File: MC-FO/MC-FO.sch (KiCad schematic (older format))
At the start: 1 part, among them J1 DB25_Female

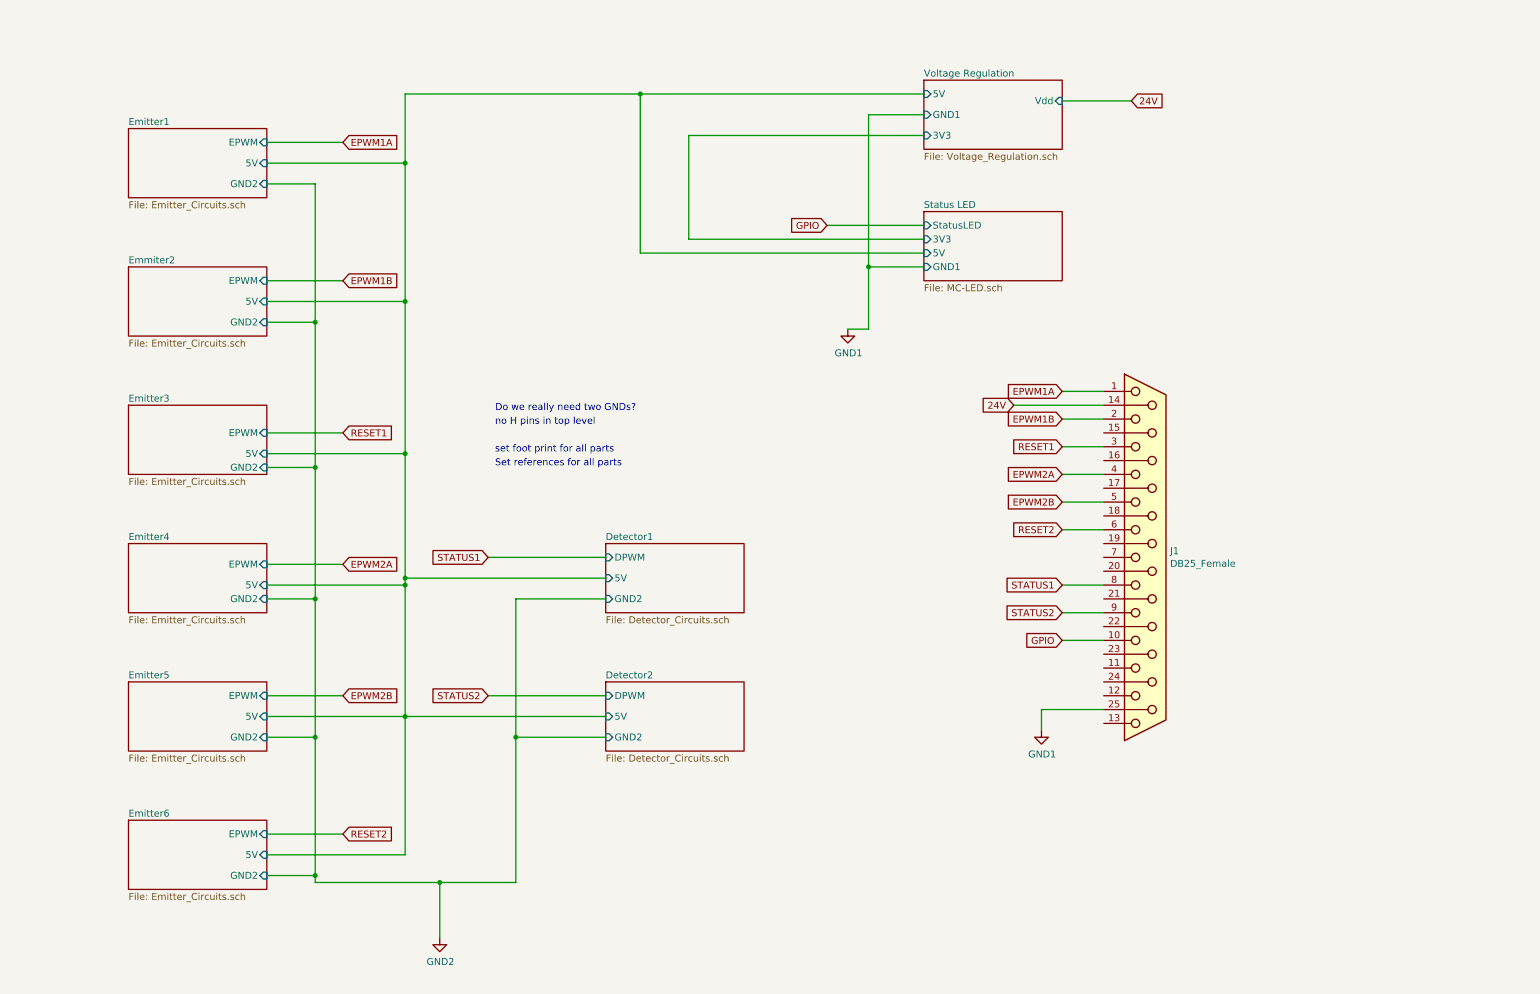
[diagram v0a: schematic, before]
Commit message: unpopulated cap after voltage regulators
and changed reference designator numbering scheme
and moved the or gate that sends 3.3 V to comparator in detector ckt
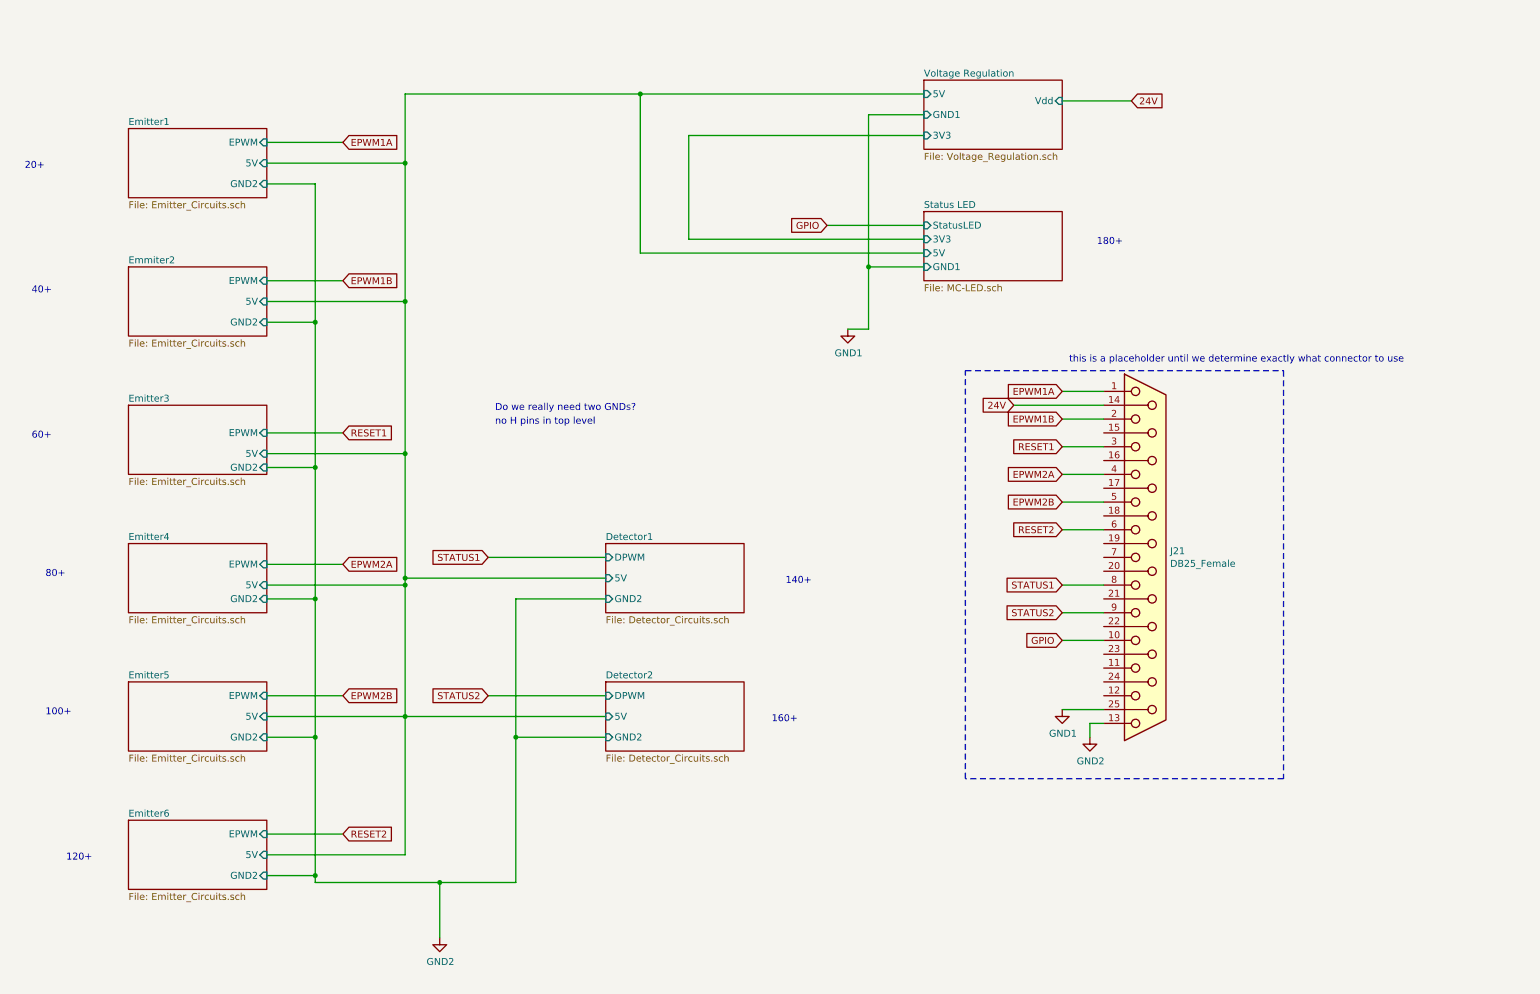
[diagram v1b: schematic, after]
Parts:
- renumbered J1 to J21
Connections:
- net GND2: now also J21.13
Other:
- note added: "100+"
- note added: "120+"
- note added: "140+"
- note added: "160+"
- note added: "180+"
- note added: "20+"
- note added: "40+"
- note added: "60+"
- note added: "80+"
- note added: "this is a placeholder until we determine exactly what connector to use"
- note removed: "Set references for all parts\n"
- note removed: "set foot print for all parts\n"
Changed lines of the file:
@@
 24V
 $Comp
-L Connector:DB25_Female J1
+L Connector:DB25_Female J21
 U 1 1 6179E2FC
 P 8850 4600
-F 0 "J1" H 9030 4646 50  0000 L CNN
+F 0 "J21" H 9030 4646 50  0000 L CNN
 F 1 "DB25_Female" H 9030 4555 50  0000 L CNN
 F 2 "Connector_Dsub:DSUB-25_Female_Horizontal_P2.77x2.54mm_EdgePinOffset9.40mm" H 8850 4600 50  0001 C CNN
@@
 	1    0    0    -1
 $EndComp
-Text Notes 4150 3850 0    50   ~ 0
-set foot print for all parts\n
-Text Notes 4150 3950 0    50   ~ 0
-Set references for all parts\n
 Text GLabel 8250 3800 0    50   Input ~ 0
 RESET1
@@
 Wire Wire Line
 	8550 5200 8250 5200
-Wire Wire Line
-	8100 5700 8550 5700
-Wire Wire Line
-	8100 5700 8100 5850
 Text GLabel 4100 4600 0    50   Input ~ 0
 STATUS1
@@
 Connection ~ 3500 2750
 $Comp
-L power:GND1 #PWR02
+L power:GND1 #PWR022
 U 1 1 617AD6F4
 P 6700 2950
-F 0 "#PWR02" H 6700 2700 50  0001 C CNN
+F 0 "#PWR022" H 6700 2700 50  0001 C CNN
 F 1 "GND1" H 6705 2777 50  0000 C CNN
 F 2 "" H 6700 2950 50  0001 C CNN
@@
 $EndComp
 $Comp
-L power:GND2 #PWR01
+L power:GND2 #PWR021
 U 1 1 617AF034
 P 3750 7350
-F 0 "#PWR01" H 3750 7100 50  0001 C CNN
+F 0 "#PWR021" H 3750 7100 50  0001 C CNN
 F 1 "GND2" H 3755 7177 50  0000 C CNN
 F 2 "" H 3750 7350 50  0001 C CNN
 F 3 "" H 3750 7350 50  0001 C CNN
 	1    3750 7350
-	1    0    0    -1
-$EndComp
-$Comp
-L power:GND1 #PWR03
-U 1 1 617AF950
-P 8100 5850
-F 0 "#PWR03" H 8100 5600 50  0001 C CNN
-F 1 "GND1" H 8105 5677 50  0000 C CNN
-F 2 "" H 8100 5850 50  0001 C CNN
-F 3 "" H 8100 5850 50  0001 C CNN
-	1    8100 5850
 	1    0    0    -1
 $EndComp
@@
 Wire Wire Line
 	2500 1600 3050 1600
+$Comp
+L power:GND1 #PWR023
+U 1 1 617AF950
+P 8250 5700
+F 0 "#PWR023" H 8250 5450 50  0001 C CNN
+F 1 "GND1" H 8255 5527 50  0000 C CNN
+F 2 "" H 8250 5700 50  0001 C CNN
+F 3 "" H 8250 5700 50  0001 C CNN
+	1    8250 5700
+	1    0    0    -1
+$EndComp
+Wire Wire Line
+	8250 5700 8550 5700
+Text Notes 8300 3200 0    50   ~ 0
+this is a placeholder until we determine exactly what connector to use
+Wire Notes Line
+	7550 3250 9850 3250
+Wire Notes Line
+	9850 3250 9850 6200
+Wire Notes Line
+	9850 6200 7550 6200
+Wire Notes Line
+	7550 6200 7550 3250
+Wire Wire Line
+	8550 5800 8450 5800
+Wire Wire Line
+	8450 5800 8450 5900
+$Comp
+L power:GND2 #PWR0102
+U 1 1 61820807
+P 8450 5900
+F 0 "#PWR0102" H 8450 5650 50  0001 C CNN
+F 1 "GND2" H 8455 5727 50  0000 C CNN
+F 2 "" H 8450 5900 50  0001 C CNN
+F 3 "" H 8450 5900 50  0001 C CNN
+	1    8450 5900
+	1    0    0    -1
+$EndComp
+Text Notes 750  1800 0    50   ~ 0
+20+
+Text Notes 800  2700 0    50   ~ 0
+40+
+Text Notes 800  3750 0    50   ~ 0
+60+
+Text Notes 900  4750 0    50   ~ 0
+80+
+Text Notes 900  5750 0    50   ~ 0
+100+
+Text Notes 1050 6800 0    50   ~ 0
+120+
+Text Notes 6250 4800 0    50   ~ 0
+140+
+Text Notes 6150 5800 0    50   ~ 0
+160+
+Text Notes 8500 2350 0    50   ~ 0
+180+
 $EndSCHEMATC

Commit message: Fixed file hierarchy
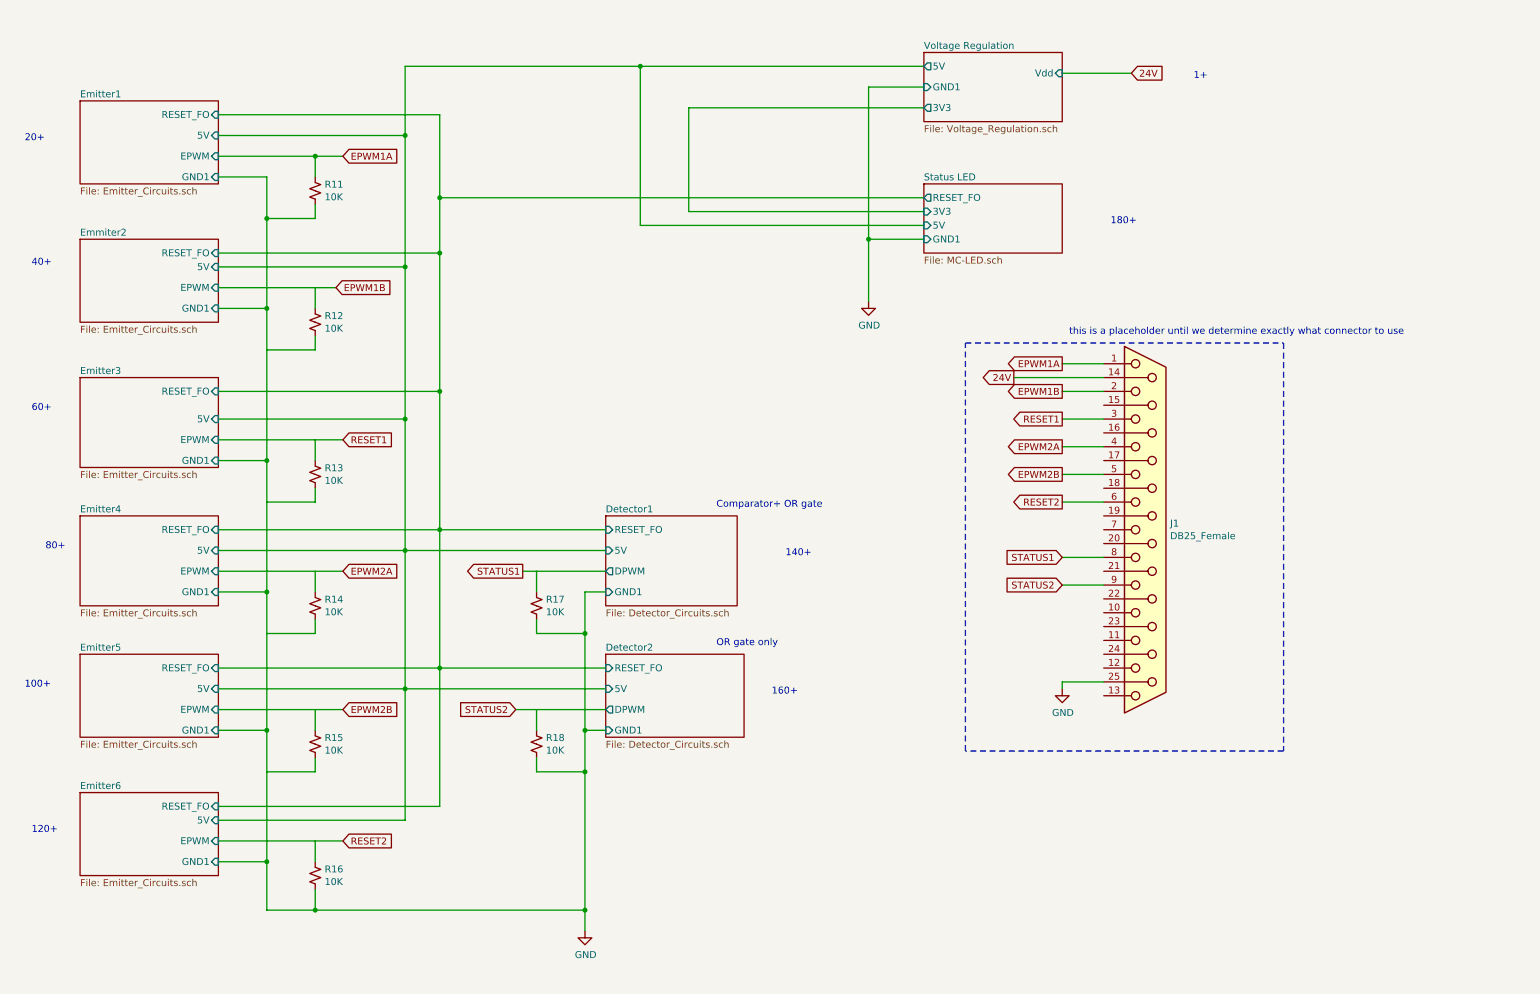
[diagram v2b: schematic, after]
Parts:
- added R11, R12, R13, R14, R15, R16, R17, R18: 10K, Resistor_SMD:R_0603_1608Metric, symbol Device:R_Small_US
- renumbered J21 to J1
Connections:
- net labels added: GND
- net labels removed: GND1, GND2, GPIO
- wire segments 69 -> 106
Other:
- note added: "1+"
- note added: "Comparator+ OR gate"
- note added: "OR gate only"
- note removed: "Do we really need two GNDs?"
- note removed: "no H pins in top level\n"
- moved on the sheet: J1

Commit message: Detector2 update, RESET integration
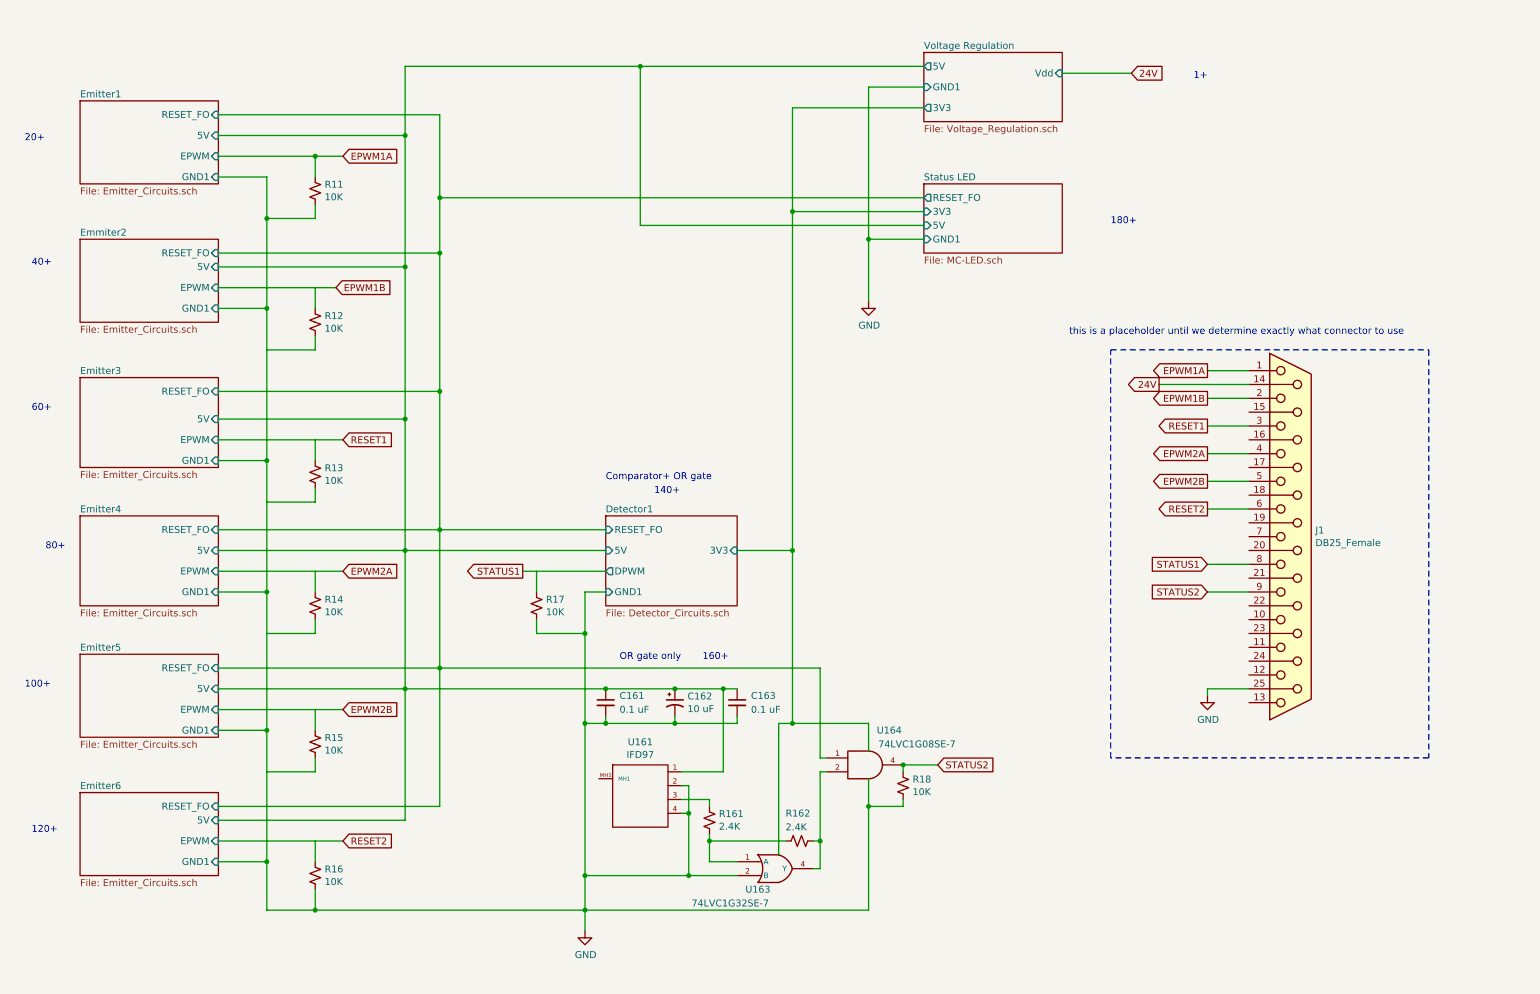
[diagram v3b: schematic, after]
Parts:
- added C161, C163: 0.1 uF, Capacitor_SMD:C_0603_1608Metric, symbol Device:C_Small
- added C162: 10 uF, Capacitor_SMD:C_0603_1608Metric, symbol Device:CP1_Small
- added R161, R162: 2.4K, Resistor_SMD:R_0603_1608Metric, symbol Device:R_Small_US
- added U161: IFD97, symbol Existing_IC_Models:IFD97
- added U163: 74LVC1G32SE-7, Package_TO_SOT_SMD:SOT-353_SC-70-5, symbol Existing_IC_Models:74LVC1G32SE-7
- added U164: 74LVC1G08SE-7, Package_TO_SOT_SMD:SOT-353_SC-70-5, symbol Existing_IC_Models:74LVC1G08SE-7
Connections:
- wire segments 106 -> 145
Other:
- moved on the sheet: J1, R18

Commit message: add connector, reset implementation
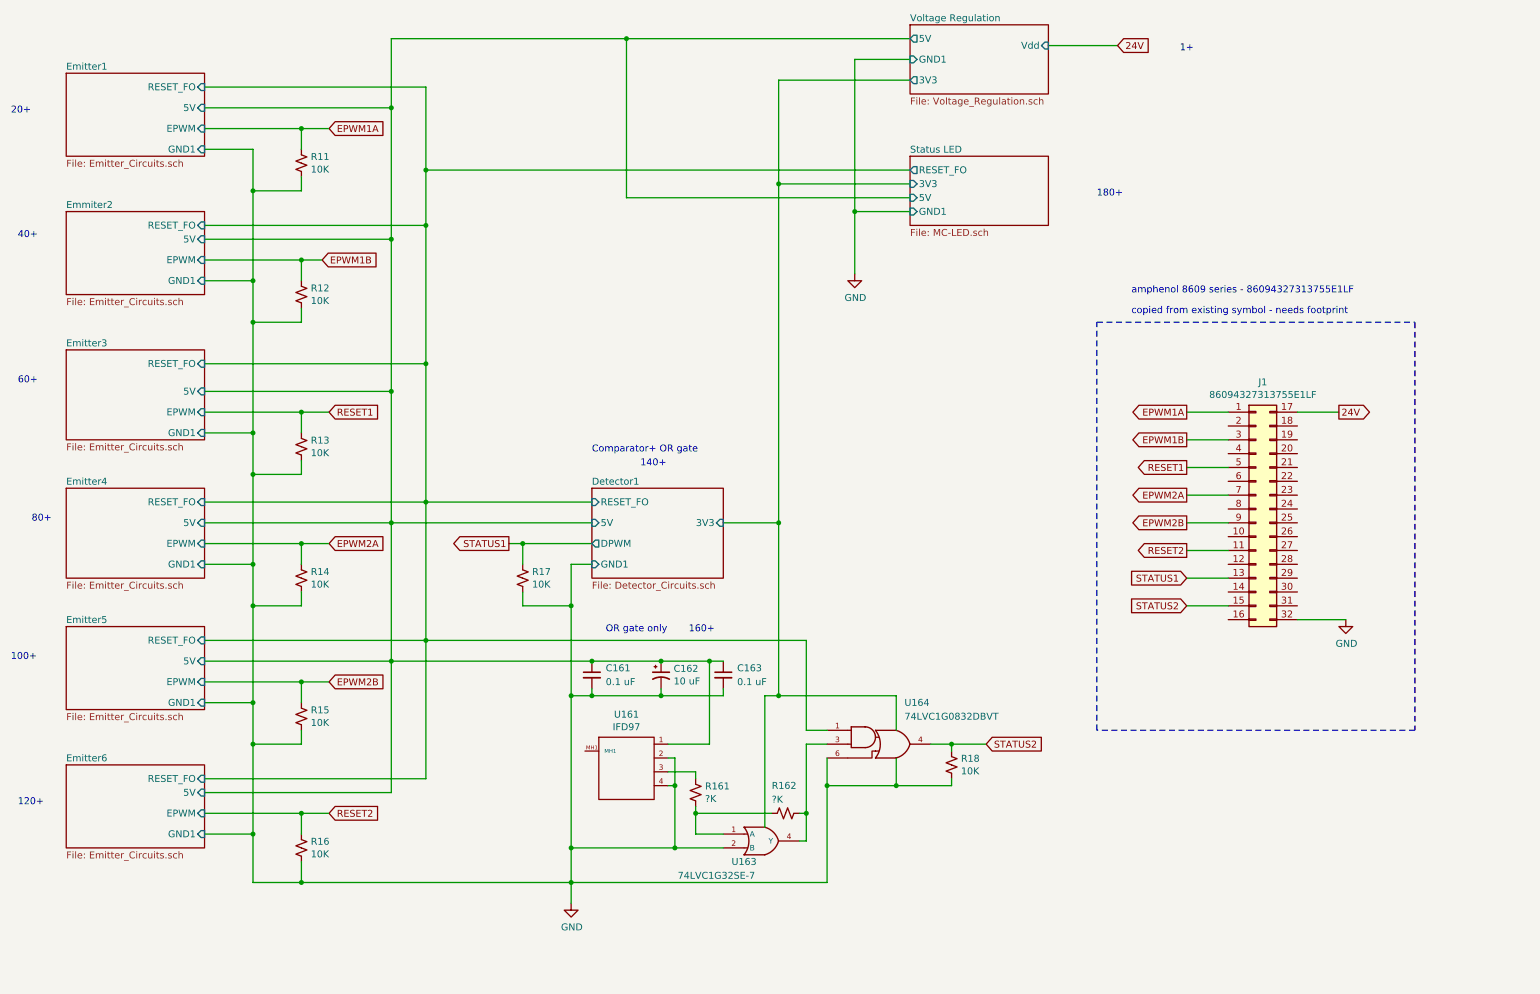
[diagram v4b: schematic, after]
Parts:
- removed J1: DB25_Female, Connector_Dsub:DSUB-25_Female_Horizontal_P2.77x2.54mm_EdgePinOffset9.40mm, symbol Connector:DB25_Female
- removed U164: 74LVC1G08SE-7, Package_TO_SOT_SMD:SOT-353_SC-70-5, symbol Existing_IC_Models:74LVC1G08SE-7
- added J1: 86094327313755E1LF, symbol Existing_IC_Models:86094327313755E1LF
- added U164: 74LVC1G0832DBVT, symbol Existing_IC_Models:74LVC1G0832DBVT
- R161, R162: value 2.4K -> ?K
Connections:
- wire segments 145 -> 157
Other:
- note added: "amphenol 8609 series - 86094327313755E1LF"
- note added: "copied from existing symbol - needs footprint\n"
- note removed: "this is a placeholder until we determine exactly what connector to use"
- moved on the sheet: C161, C162, C163, R11, R12, R13, R14, R15, R16, R161, R162, R17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

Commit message: update footprints, resistors
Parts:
- R161, R162: value ?K -> 2K
- U161: footprint (none) -> Footprints_MC-FO:IFE98
- U164: footprint (none) -> Package_TO_SOT_SMD:SOT-23-6
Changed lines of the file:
@@
 F 0 "U161" H 5100 7365 50  0000 C CNN
 F 1 "IFD97" H 5100 7274 50  0000 C CNN
-F 2 "" H 5100 7350 50  0001 C CNN
+F 2 "Footprints_MC-FO:IFE98" H 5100 7350 50  0001 C CNN
 F 3 "" H 5100 7350 50  0001 C CNN
 	1    5100 6550
@@
 P 5600 6300
 F 0 "R161" H 5668 6346 50  0000 L CNN
-F 1 "?K" H 5668 6255 50  0000 L CNN
+F 1 "2K" H 5668 6255 50  0000 L CNN
 F 2 "Resistor_SMD:R_0603_1608Metric" H 5600 6300 50  0001 C CNN
 F 3 "~" H 5600 6300 50  0001 C CNN
@@
 P 6250 6450
 F 0 "R162" V 6050 6350 50  0000 L CNN
-F 1 "?K" V 6150 6350 50  0000 L CNN
+F 1 "2K" V 6150 6350 50  0000 L CNN
 F 2 "Resistor_SMD:R_0603_1608Metric" H 6250 6450 50  0001 C CNN
 F 3 "~" H 6250 6450 50  0001 C CNN
@@
 F 0 "U164" H 7200 6250 50  0000 C CNN
 F 1 "74LVC1G0832DBVT" H 7450 6150 50  0000 C CNN
-F 2 "" H 6900 5950 50  0001 C CNN
+F 2 "Package_TO_SOT_SMD:SOT-23-6" H 6900 5950 50  0001 C CNN
 F 3 "http://www.ti.com/lit/sg/scyt129e/scyt129e.pdf" H 6900 5950 50  0001 C CNN
 	1    6900 5950

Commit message: Linked footprint for connector
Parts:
- J1: footprint (none) -> Footprints_MC-FO:86094327313755E1LF
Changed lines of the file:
@@
 F 0 "J1" H 9700 5167 50  0000 C CNN
 F 1 "86094327313755E1LF" H 9700 5076 50  0000 C CNN
-F 2 "" H 9650 4250 50  0001 C CNN
+F 2 "Footprints_MC-FO:86094327313755E1LF" H 9650 4250 50  0001 C CNN
 F 3 "~" H 9650 4250 50  0001 C CNN
 	1    9650 4250
